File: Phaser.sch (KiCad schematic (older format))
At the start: 114 parts, among them J1 9V, J10 DUALB, J11 BYPASSC, J12 Dry, J13 BYPASSB, J14 DUALC, J15 GND, J16 BYPASSA, J17 PHASE/VIBEA, J18 PHASE/VIBEC, J19 Out, J2 In, J20 GND, J21 GND, J3 GND, J4 DUALA, J5 P1SCN, J6 P1TIP, J7 P2SCN, J8 P2TIP, J9 PHASE/VIBEB, SW1 SLOW, SW2 SQUARE, SW3 SW_Rotary4x3, SW4 SW_Rotary4x3, U1 TL074, U2 TL074, U3 TL072, U4 TL072

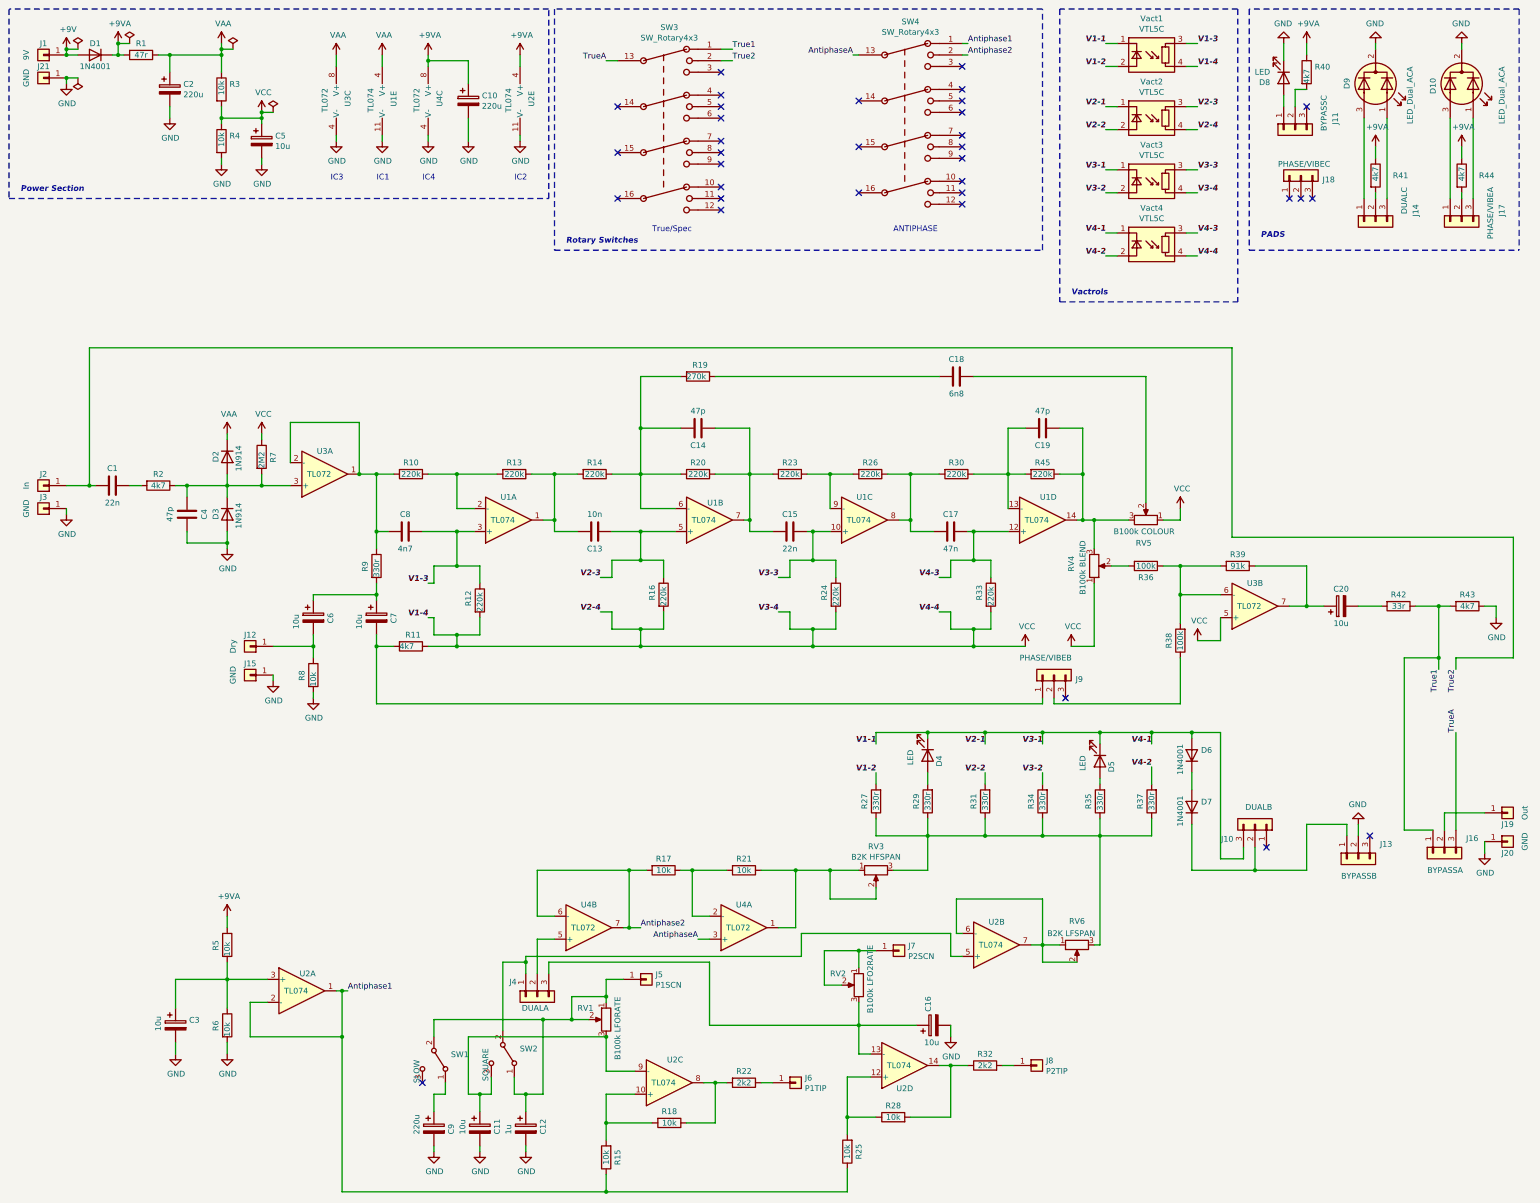
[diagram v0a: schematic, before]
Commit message: Fixed initial errors and laid out 1590XX pcb
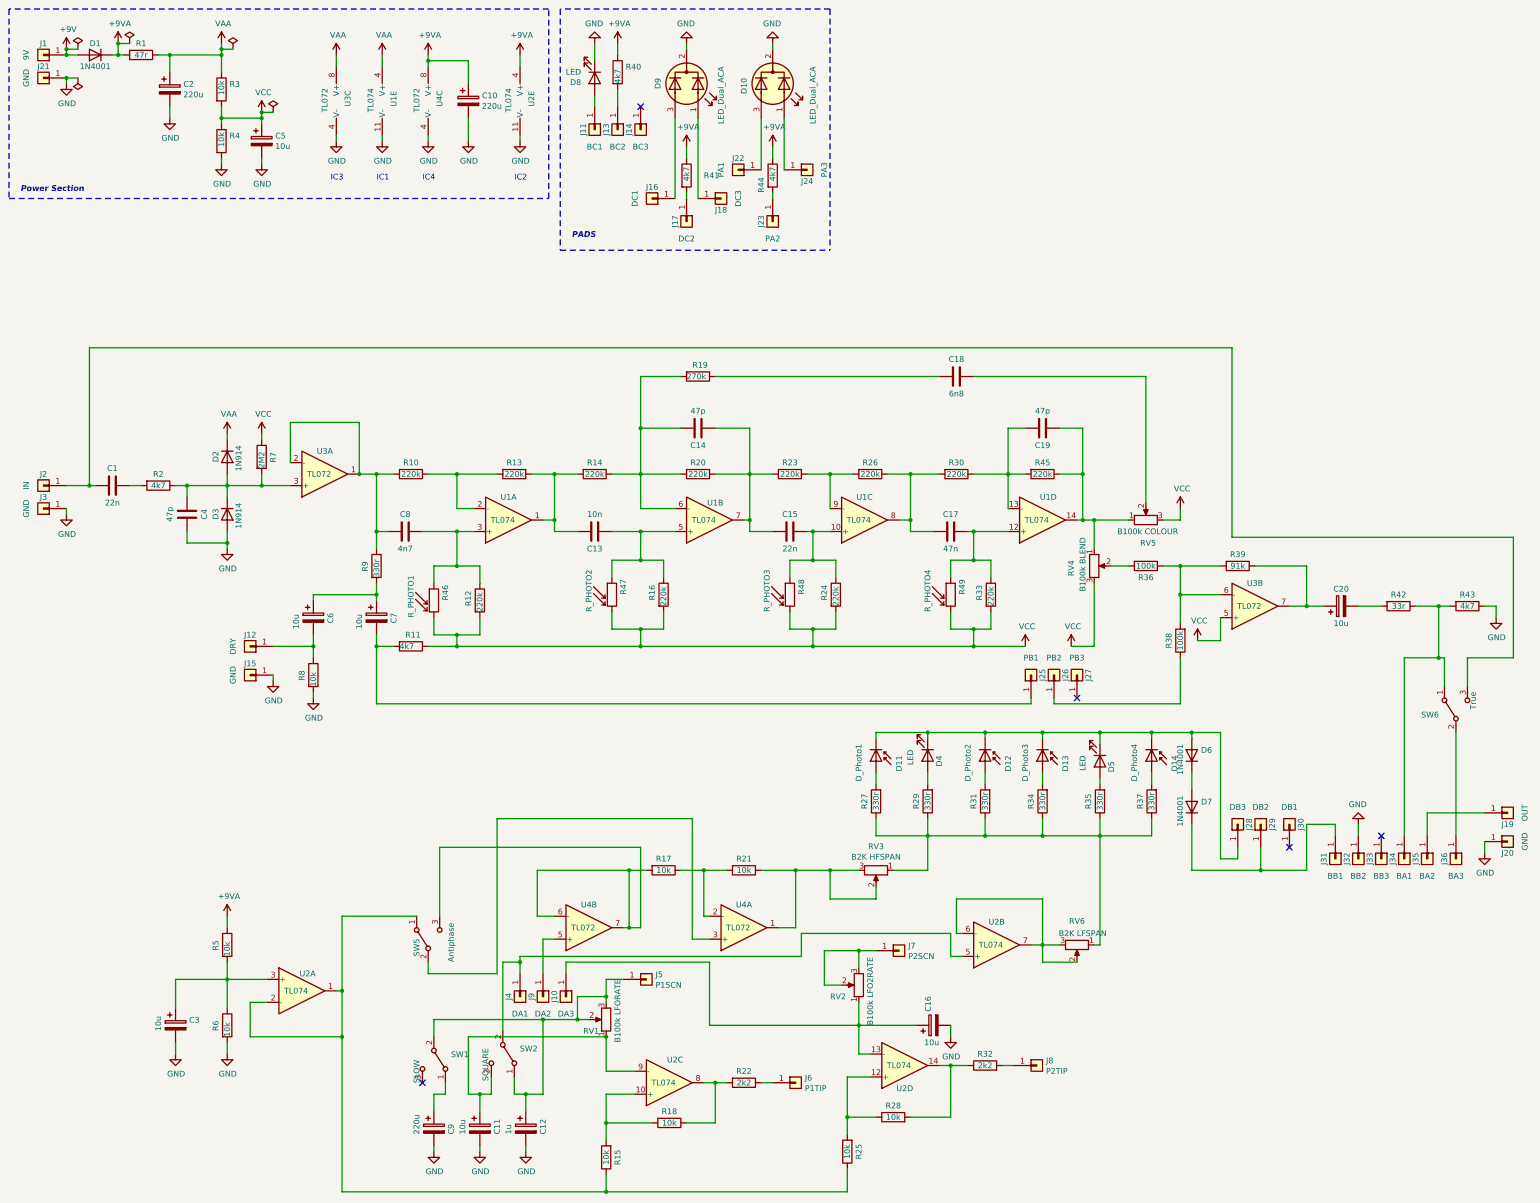
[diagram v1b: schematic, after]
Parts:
- removed J10: DUALB, Connector_Wire:SolderWire-0.25sqmm_1x03_P4.2mm_D0.65mm_OD1.7mm, symbol Connector_Generic:Conn_01x03
- removed J11: BYPASSC, Connector_Wire:SolderWire-0.25sqmm_1x03_P4.2mm_D0.65mm_OD1.7mm, symbol Connector_Generic:Conn_01x03
- removed J13: BYPASSB, Connector_Wire:SolderWire-0.25sqmm_1x03_P4.2mm_D0.65mm_OD1.7mm, symbol Connector_Generic:Conn_01x03
- removed J14: DUALC, Connector_Wire:SolderWire-0.25sqmm_1x03_P4.2mm_D0.65mm_OD1.7mm, symbol Connector_Generic:Conn_01x03
- removed J16: BYPASSA, Connector_Wire:SolderWire-0.25sqmm_1x03_P4.2mm_D0.65mm_OD1.7mm, symbol Connector_Generic:Conn_01x03
- removed J17: PHASE/VIBEA, Connector_Wire:SolderWire-0.25sqmm_1x03_P4.2mm_D0.65mm_OD1.7mm, symbol Connector_Generic:Conn_01x03
- removed J18: PHASE/VIBEC, Connector_Wire:SolderWire-0.25sqmm_1x03_P4.2mm_D0.65mm_OD1.7mm, symbol Connector_Generic:Conn_01x03
- removed J4: DUALA, Connector_Wire:SolderWire-0.25sqmm_1x03_P4.2mm_D0.65mm_OD1.7mm, symbol Connector_Generic:Conn_01x03
- removed J9: PHASE/VIBEB, Connector_Wire:SolderWire-0.25sqmm_1x03_P4.2mm_D0.65mm_OD1.7mm, symbol Connector_Generic:Conn_01x03
- removed SW3, SW4: SW_Rotary4x3, MyLibrary:LORINCK1049, symbol Switch:SW_Rotary4x3
- removed Vact1, Vact2, Vact3, Vact4: VTL5C, OptoDevice:PerkinElmer_VTL5C, symbol Isolator:VTL5C
- added D11: D_Photo1, MyLibrary:LED_D5.0mm, symbol Device:D_Photo
- added D12: D_Photo2, MyLibrary:LED_D5.0mm, symbol Device:D_Photo
- added D13: D_Photo3, MyLibrary:LED_D5.0mm, symbol Device:D_Photo
- added D14: D_Photo4, MyLibrary:LED_D5.0mm, symbol Device:D_Photo
- added J10: DA3, Connector_Wire:SolderWire-0.25sqmm_1x01_D0.65mm_OD1.7mm, symbol Connector_Generic:Conn_01x01
- added J11: BC1, Connector_Wire:SolderWire-0.25sqmm_1x01_D0.65mm_OD1.7mm, symbol Connector_Generic:Conn_01x01
- added J13: BC2, Connector_Wire:SolderWire-0.25sqmm_1x01_D0.65mm_OD1.7mm, symbol Connector_Generic:Conn_01x01
- added J14: BC3, Connector_Wire:SolderWire-0.25sqmm_1x01_D0.65mm_OD1.7mm, symbol Connector_Generic:Conn_01x01
- added J16: DC1, Connector_Wire:SolderWire-0.25sqmm_1x01_D0.65mm_OD1.7mm, symbol Connector_Generic:Conn_01x01
- added J17: DC2, Connector_Wire:SolderWire-0.25sqmm_1x01_D0.65mm_OD1.7mm, symbol Connector_Generic:Conn_01x01
- added J18: DC3, Connector_Wire:SolderWire-0.25sqmm_1x01_D0.65mm_OD1.7mm, symbol Connector_Generic:Conn_01x01
- added J22: PA1, Connector_Wire:SolderWire-0.25sqmm_1x01_D0.65mm_OD1.7mm, symbol Connector_Generic:Conn_01x01
- added J23: PA2, Connector_Wire:SolderWire-0.25sqmm_1x01_D0.65mm_OD1.7mm, symbol Connector_Generic:Conn_01x01
- added J24: PA3, Connector_Wire:SolderWire-0.25sqmm_1x01_D0.65mm_OD1.7mm, symbol Connector_Generic:Conn_01x01
- added J25: PB1, Connector_Wire:SolderWire-0.25sqmm_1x01_D0.65mm_OD1.7mm, symbol Connector_Generic:Conn_01x01
- added J26: PB2, Connector_Wire:SolderWire-0.25sqmm_1x01_D0.65mm_OD1.7mm, symbol Connector_Generic:Conn_01x01
- added J27: PB3, Connector_Wire:SolderWire-0.25sqmm_1x01_D0.65mm_OD1.7mm, symbol Connector_Generic:Conn_01x01
- added J28: DB3, Connector_Wire:SolderWire-0.25sqmm_1x01_D0.65mm_OD1.7mm, symbol Connector_Generic:Conn_01x01
- added J29: DB2, Connector_Wire:SolderWire-0.25sqmm_1x01_D0.65mm_OD1.7mm, symbol Connector_Generic:Conn_01x01
- added J30: DB1, Connector_Wire:SolderWire-0.25sqmm_1x01_D0.65mm_OD1.7mm, symbol Connector_Generic:Conn_01x01
- added J31: BB1, Connector_Wire:SolderWire-0.25sqmm_1x01_D0.65mm_OD1.7mm, symbol Connector_Generic:Conn_01x01
- added J32: BB2, Connector_Wire:SolderWire-0.25sqmm_1x01_D0.65mm_OD1.7mm, symbol Connector_Generic:Conn_01x01
- added J33: BB3, Connector_Wire:SolderWire-0.25sqmm_1x01_D0.65mm_OD1.7mm, symbol Connector_Generic:Conn_01x01
- added J34: BA1, Connector_Wire:SolderWire-0.25sqmm_1x01_D0.65mm_OD1.7mm, symbol Connector_Generic:Conn_01x01
- added J35: BA2, Connector_Wire:SolderWire-0.25sqmm_1x01_D0.65mm_OD1.7mm, symbol Connector_Generic:Conn_01x01
- added J36: BA3, Connector_Wire:SolderWire-0.25sqmm_1x01_D0.65mm_OD1.7mm, symbol Connector_Generic:Conn_01x01
- added J4: DA1, Connector_Wire:SolderWire-0.25sqmm_1x01_D0.65mm_OD1.7mm, symbol Connector_Generic:Conn_01x01
- added J9: DA2, Connector_Wire:SolderWire-0.25sqmm_1x01_D0.65mm_OD1.7mm, symbol Connector_Generic:Conn_01x01
- added R46: R_PHOTO1, OptoDevice:R_LDR_5.2x5.2mm_P3.5mm_Horizontal, symbol Device:R_PHOTO
- added R47: R_PHOTO2, OptoDevice:R_LDR_5.2x5.2mm_P3.5mm_Horizontal, symbol Device:R_PHOTO
- added R48: R_PHOTO3, OptoDevice:R_LDR_5.2x5.2mm_P3.5mm_Horizontal, symbol Device:R_PHOTO
- added R49: R_PHOTO4, OptoDevice:R_LDR_5.2x5.2mm_P3.5mm_Horizontal, symbol Device:R_PHOTO
- added SW5: Antiphase, MyLibrary:SWITCH_SPDT_PTH_12.9X6.9MM, symbol Switch:SW_SPDT
- added SW6: True, MyLibrary:SWITCH_SPDT_PTH_12.9X6.9MM, symbol Switch:SW_SPDT
- D4, D5, D8: footprint LED_THT:LED_D5.0mm -> MyLibrary:LED_D5.0mm
- J12: value Dry -> DRY
- J19: value Out -> OUT
- J2: value In -> IN
- SW1, SW2: footprint Switches:SWITCH_SPDT_PTH_11.6X4.0MM -> MyLibrary:SWITCH_SPDT_PTH_12.9X6.9MM
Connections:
- net GND: now also J32.1 (Pin_1)
- net VCC: now also RV4.3, RV5.3, R46.2, R47.2, R48.2, R49.2; no longer RV4.1, RV5.1
- net at C7.2, R11.2: now also J25.1 (Pin_1)
- net at D9.1 (A1): now also J18.1 (Pin_1)
- net at D9.3 (A2): now also J16.1 (Pin_1)
- net at D10.1 (A1): now also J24.1 (Pin_1)
- net at D10.3 (A2): now also J22.1 (Pin_1)
- net at C19.2, R45.1, U1.14: now also RV4.1, RV5.1; no longer RV4.3, RV5.3
- net at J19.1 (Pin_1): now also J35.1 (Pin_1)
- net at D7.1 (K): now also J29.1 (Pin_1), J31.1 (Pin_1)
- net at D8.2 (A): now also J11.1 (Pin_1)
- net at R40.2: now also J13.1 (Pin_1)
- net at R38.1: now also J26.1 (Pin_1)
- net at R44.2: now also J23.1 (Pin_1)
- net at R27.1, R29.1, R31.1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: now also RV3.1, RV6.1; no longer RV3.3, RV6.3
- net at R21.1, RV3.2, U4.1: now also RV3.3; no longer RV3.1
- net at U4.5 (+): now also J9.1 (Pin_1)
- net at SW2.2 (B), U2.5 (+): now also J4.1 (Pin_1)
- net at C16.1, U2.13 (-): now also RV2.1, J10.1 (Pin_1); no longer RV2.3
- net at C12.1, J5.1 (Pin_1), RV1.2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: now also RV1.3; no longer RV1.1
- net at C11.1, SW2.3 (C), U2.9 (-): now also RV1.1; no longer RV1.3
- net at J7.1 (Pin_1), RV2.2: now also RV2.3; no longer RV2.1
- net at RV6.2, U2.6 (-), U2.7: now also RV6.3; no longer RV6.1
- net at R41.2: now also J17.1 (Pin_1)
- net Antiphase1: no longer names the net of R15.1, R25.1, U2.1, U2.2 (-)
- net Antiphase1: now also SW5.1 (A)
- net Antiphase2: no longer names the net of R17.2, U4.6 (-), U4.7
- net Antiphase2: now also SW5.3 (C)
- net AntiphaseA: no longer names the net of U4.3 (+)
- net AntiphaseA: now also SW5.2 (B)
- net True1: no longer names the net of R42.1, R43.2
- net True1: now also J34.1 (Pin_1), SW6.1 (A)
- net True2: no longer names the net of C1.2, J2.1 (Pin_1)
- net True2: now also SW6.3 (C)
- net V1-1: no longer names the net of D4.1 (K), D5.1 (K), D6.2 (A)
- net V1-1: now also D11.1 (K), D12.1 (K), D13.1 (K), D14.1 (K), J28.1 (Pin_1)
- net V1-2: no longer names the net of R27.2
- net V1-2: now also D11.2 (A)
- net V1-3: no longer names the net of C8.1, R12.1, U1.3 (+)
- net V1-3: now also R46.1
- net V2-2: no longer names the net of R31.2
- net V2-2: now also D12.2 (A)
- net V2-3: no longer names the net of C13.2, R16.1, U1.5 (+)
- net V2-3: now also R47.1
- net V3-2: no longer names the net of R34.2
- net V3-2: now also D13.2 (A)
- net V3-3: no longer names the net of C15.1, R24.1, U1.10 (+)
- net V3-3: now also R48.1
- net V4-2: no longer names the net of R37.2
- net V4-2: now also D14.2 (A)
- net V4-3: no longer names the net of C17.1, R33.1, U1.12 (+)
- net V4-3: now also R49.1
- new net: J36.1 (Pin_1), SW6.2 (B)
- no-connect marks 34 -> 5
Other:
- note removed: "ANTIPHASE"
- note removed: "Rotary Switches"
- note removed: "True/Spec"
- note removed: "Vactrols"
- moved on the sheet: D10, D8, D9, R40, R41, R44

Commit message: Deleted connection between R31 R34
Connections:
- net at R34.1, R35.1, R37.1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: no longer R27.1, R29.1, R31.1, RV3.1
- new net: R27.1, R29.1, R31.1, RV3.1
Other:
- moved on the sheet: SW5
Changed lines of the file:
@@
 Wire Wire Line
 	9050 7550 9050 7700
-Wire Wire Line
-	9050 7700 9550 7700
-Connection ~ 9550 7700
 $Comp
 L Device:R R29
@@
 Wire Wire Line
 	8550 7700 9050 7700
-Connection ~ 9050 7700
 $Comp
 L Device:R R27
@@
 $EndComp
 Wire Wire Line
-	4850 9400 4850 8800
-Wire Wire Line
-	4850 8800 5000 8800
+	4850 9400 4850 8850
 NoConn ~ 4150 9850
 $Comp
@@
 L Switch:SW_SPDT SW5
 U 1 1 5FB9D562
-P 4200 8600
-F 0 "SW5" H 4050 8700 50  0000 L CNN
-F 1 "Antiphase" H 4000 8400 50  0000 L CNN
-F 2 "MyLibrary:SWITCH_SPDT_PTH_12.9X6.9MM" H 4200 8600 50  0001 C CNN
-F 3 "~" H 4200 8600 50  0001 C CNN
-	1    4200 8600
-	0    -1   -1   0
-$EndComp
-Wire Wire Line
-	4100 8400 3450 8400
-Wire Wire Line
-	3450 8400 3450 9050
+P 4200 8500
+F 0 "SW5" H 4050 8600 50  0000 L CNN
+F 1 "Antiphase" H 4000 8300 50  0000 L CNN
+F 2 "MyLibrary:SWITCH_SPDT_PTH_12.9X6.9MM" H 4200 8500 50  0001 C CNN
+F 3 "~" H 4200 8500 50  0001 C CNN
+	1    4200 8500
+	0    1    1    0
+$EndComp
 Wire Wire Line
 	6050 7800 6050 8500
@@
 Connection ~ 5950 8500
 Wire Wire Line
-	4300 8400 4300 7800
-Wire Wire Line
-	4300 7800 6050 7800
-Wire Wire Line
-	4200 8800 4200 8900
-Wire Wire Line
-	4200 8900 4800 8900
-Wire Wire Line
-	4800 8900 4800 7550
-Wire Wire Line
 	6600 8400 6600 8000
 Connection ~ 6600 8000
@@
 Wire Wire Line
 	6400 8000 6600 8000
-Wire Wire Line
-	6500 8600 6500 7550
-Wire Wire Line
-	6500 8600 6650 8600
-Wire Wire Line
-	4800 7550 6500 7550
 $Comp
 L Connector_Generic:Conn_01x01 J34
@@
 $EndComp
 Wire Wire Line
-	5000 8800 5000 8900
-Connection ~ 5000 8800
-Wire Wire Line
-	5000 8800 5000 8750
-Wire Wire Line
 	5000 8750 7450 8750
 Wire Wire Line
@@
 Wire Wire Line
 	5400 8800 6650 8800
+Wire Wire Line
+	5000 8850 4850 8850
+Connection ~ 5000 8850
+Wire Wire Line
+	5000 8850 5000 8900
+Wire Wire Line
+	5000 8750 5000 8850
+Wire Wire Line
+	6350 8600 6650 8600
+Wire Wire Line
+	4200 8300 4200 8150
+Wire Wire Line
+	4200 8150 6350 8150
+Wire Wire Line
+	6350 8150 6350 8600
+Wire Wire Line
+	4300 8700 4300 9050
+Wire Wire Line
+	4300 9050 3450 9050
+Wire Wire Line
+	4100 8700 4100 8800
+Wire Wire Line
+	4100 8800 3700 8800
+Wire Wire Line
+	3700 8800 3700 7800
+Wire Wire Line
+	3700 7800 6050 7800
 $EndSCHEMATC

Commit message: Provisional Phaser V2.0 completion
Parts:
- R42: value 33r -> 330r
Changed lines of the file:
@@
 P 12650 5700
 F 0 "R42" V 12550 5700 50  0000 C CNN
-F 1 "33r" V 12650 5700 50  0000 C CNN
+F 1 "330r" V 12650 5700 50  0000 C CNN
 F 2 "Resistor_THT:R_Axial_DIN0207_L6.3mm_D2.5mm_P7.62mm_Horizontal" V 12580 5700 50  0001 C CNN
 F 3 "~" H 12650 5700 50  0001 C CNN
